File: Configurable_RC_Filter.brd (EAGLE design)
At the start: 48.3 x 40.6 mm, 76 parts, among them SW1 DIP-06, SW2 DIP-06, SW3 DIP-06, SW4 DIP-06

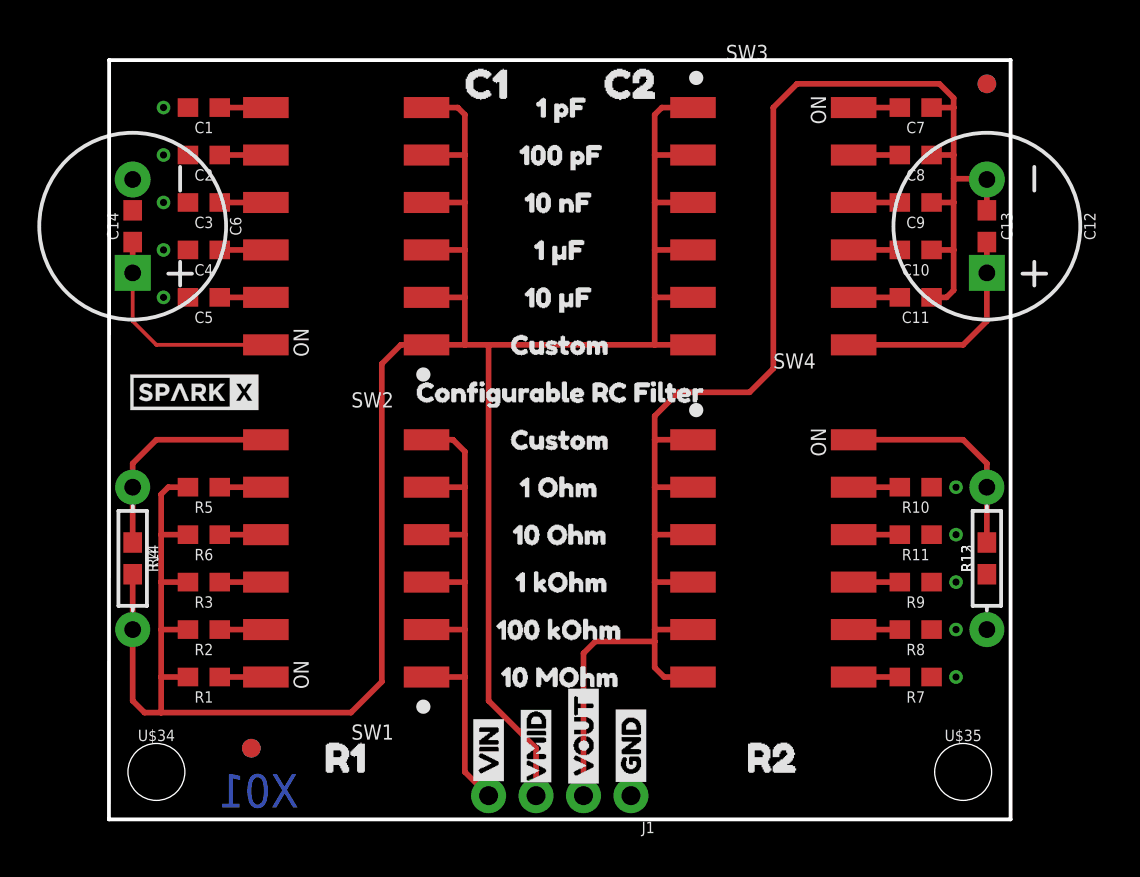
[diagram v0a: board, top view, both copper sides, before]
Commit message: Change cap to NS package.
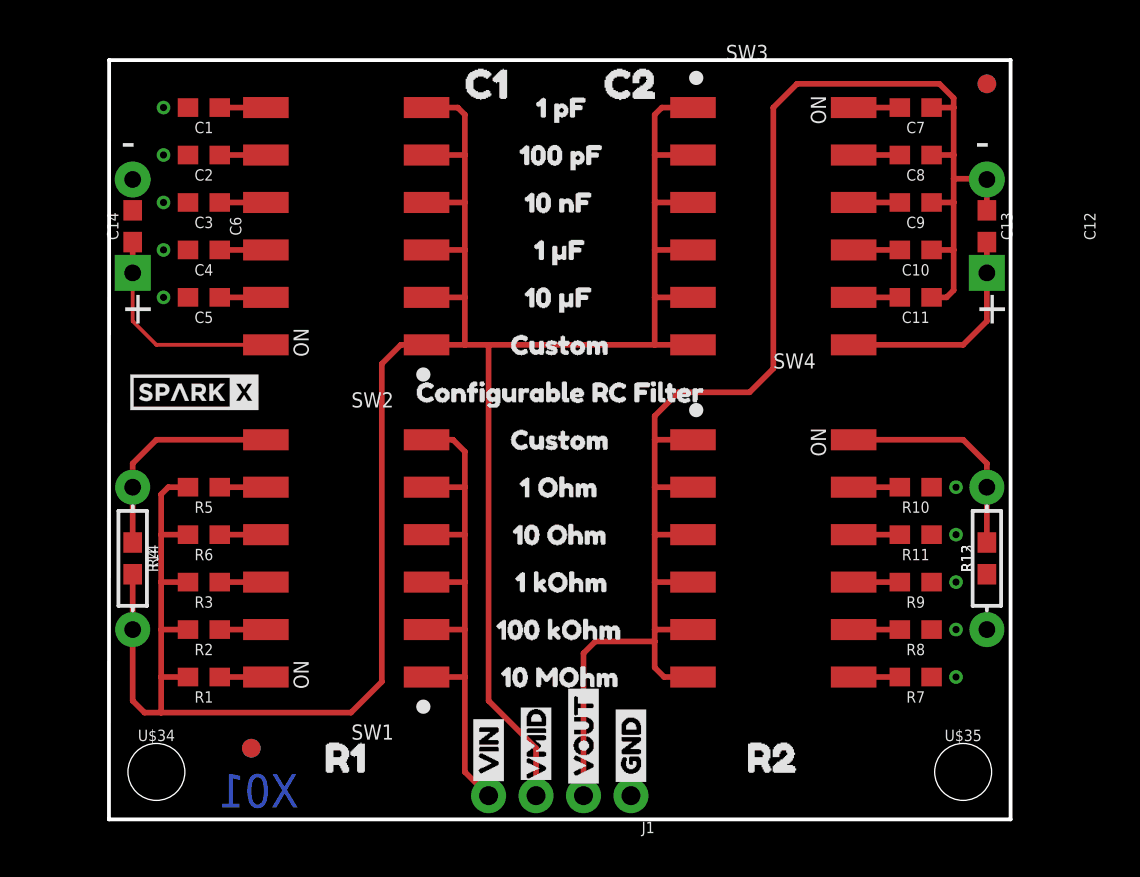
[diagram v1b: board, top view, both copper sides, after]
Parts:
- C12, C6: value 1mF -> 1000UF-RADIAL-5MM-25V-20%-NO-SILK; device SparkFun-Capacitors:CPOL-RADIAL-5MM-10MM -> SparkFun-Capacitors:CPOL-RADIAL-5MM-10MM-NS
- moved U$10 0.13 mm to (22.9, 1.27)
- moved U$9 0.13 mm to (22.9, 1.27)
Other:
- board text added: "+"
- board text added: "-"
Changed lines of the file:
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@@
 <text x="10.16" y="0.635" size="1.778" layer="16" font="vector" ratio="15" rot="MR0">X01</text>
 <text x="25.4" y="-8.89" size="1.778" layer="51" font="vector" ratio="10">Andy England</text>
+<text x="46.355" y="26.543" size="1.778" layer="21" font="vector" ratio="15">+</text>
+<text x="0.635" y="26.543" size="1.778" layer="21" font="vector" ratio="15">+</text>
+<text x="0.635" y="35.433" size="1.778" layer="21" font="vector" ratio="15">-</text>
+<text x="46.355" y="35.433" size="1.778" layer="21" font="vector" ratio="15">-</text>
 </plain>
 <attributes>
@@
 <attribute name="VALUE" x="5.08" y="28.702" size="0.6096" layer="27" font="vector" ratio="20" rot="R180" align="top-center"/>
 </element>
-<element name="C6" library="SparkFun-Capacitors" package="CPOL-RADIAL-5MM-10MM" value="1mF" x="1.27" y="31.75" smashed="yes" rot="R270">
+<element name="C6" library="SparkFun-Capacitors" package="CPOL-RADIAL-5MM-10MM-NS" value="1000UF-RADIAL-5MM-25V-20%-NO-SILK" x="1.27" y="31.75" smashed="yes" rot="R270">
 <attribute name="NAME" x="6.477" y="31.75" size="0.6096" layer="25" font="vector" ratio="20" rot="R270" align="bottom-center"/>
-<attribute name="PROD_ID" value="CAP-09538" x="1.27" y="31.75" size="1.778" layer="27" rot="R270" display="off"/>
-<attribute name="VALUE" x="-3.937" y="31.75" size="0.6096" layer="27" font="vector" ratio="20" rot="R270" align="top-center"/>
 </element>
 <element name="SW3" library="SparkFun-Switches" package="DIPSWITCH-06-SMD" value="DIP-06" x="35.56" y="31.75" smashed="yes" rot="R270">
@@
 <attribute name="VALUE" x="43.18" y="28.702" size="0.6096" layer="27" font="vector" ratio="20" rot="R180" align="top-center"/>
 </element>
-<element name="C12" library="SparkFun-Capacitors" package="CPOL-RADIAL-5MM-10MM" value="1mF" x="46.99" y="31.75" smashed="yes" rot="R270">
+<element name="C12" library="SparkFun-Capacitors" package="CPOL-RADIAL-5MM-10MM-NS" value="1000UF-RADIAL-5MM-25V-20%-NO-SILK" x="46.99" y="31.75" smashed="yes" rot="R270">
 <attribute name="NAME" x="52.197" y="31.75" size="0.6096" layer="25" font="vector" ratio="20" rot="R270" align="bottom-center"/>
-<attribute name="PROD_ID" value="CAP-09538" x="30.48" y="43.18" size="1.778" layer="27" rot="R270" display="off"/>
-<attribute name="VALUE" x="41.783" y="31.75" size="0.6096" layer="27" font="vector" ratio="20" rot="R270" align="top-center"/>
 </element>
 <element name="SW4" library="SparkFun-Switches" package="DIPSWITCH-06-SMD" value="DIP-06" x="35.56" y="13.97" smashed="yes" rot="R270">
@@
 <element name="U$7" library="buzzard_labels (7)" package="VIN1" value="" x="20.32" y="1.524" smashed="yes" rot="R90"/>
 <element name="U$8" library="buzzard_labels (7)" package="VIN1" value="" x="20.32" y="1.524" smashed="yes" rot="MR90"/>
-<element name="U$9" library="buzzard_labels (7)" package="VMID3" value="" x="22.86" y="1.143" smashed="yes" rot="R90"/>
-<element name="U$10" library="buzzard_labels (7)" package="VMID3" value="" x="22.86" y="1.143" smashed="yes" rot="MR90"/>
+<element name="U$9" library="buzzard_labels (7)" package="VMID3" value="" x="22.86" y="1.27" smashed="yes" rot="R90"/>
+<element name="U$10" library="buzzard_labels (7)" package="VMID3" value="" x="22.86" y="1.27" smashed="yes" rot="MR90"/>
 <element name="U$11" library="buzzard_labels (8)" package="VOUT3" value="" x="25.4" y="1.397" smashed="yes" rot="R90"/>
 <element name="U$12" library="buzzard_labels (8)" package="VOUT3" value="" x="25.4" y="1.397" smashed="yes" rot="MR90"/>
@@
 <contactref element="R13" pad="1"/>
 <contactref element="C14" pad="2"/>
+<wire x1="44.03" y1="17.78" x2="45.339" y2="17.78" width="0" layer="19" extent="1-1"/>
+<wire x1="45.339" y1="15.24" x2="45.339" y2="17.78" width="0" layer="19" extent="1-1"/>
+<wire x1="44.03" y1="15.24" x2="45.339" y2="15.24" width="0" layer="19" extent="1-1"/>
+<wire x1="45.339" y1="12.7" x2="45.339" y2="15.24" width="0" layer="19" extent="1-1"/>
+<wire x1="44.03" y1="12.7" x2="45.339" y2="12.7" width="0" layer="19" extent="1-1"/>
+<wire x1="46.99" y1="13.12" x2="45.339" y2="12.7" width="0" layer="19" extent="1-1"/>
+<wire x1="45.339" y1="10.16" x2="45.339" y2="12.7" width="0" layer="19" extent="1-1"/>
+<wire x1="44.03" y1="10.16" x2="45.339" y2="10.16" width="0" layer="19" extent="1-1"/>
+<wire x1="46.99" y1="10.16" x2="45.339" y2="10.16" width="0" layer="19" extent="1-1"/>
+<wire x1="45.339" y1="7.62" x2="45.339" y2="10.16" width="0" layer="19" extent="1-1"/>
+<wire x1="44.03" y1="7.62" x2="45.339" y2="7.62" width="0" layer="19" extent="1-1"/>
+<wire x1="27.94" y1="1.27" x2="44.03" y2="7.62" width="0" layer="19" extent="1-1"/>
+<wire x1="4.23" y1="27.94" x2="27.94" y2="1.27" width="0" layer="19" extent="1-1"/>
+<wire x1="2.921" y1="27.94" x2="4.23" y2="27.94" width="0" layer="19" extent="1-1"/>
+<wire x1="4.23" y1="30.48" x2="4.23" y2="27.94" width="0" layer="19" extent="1-1"/>
+<wire x1="2.921" y1="30.48" x2="4.23" y2="30.48" width="0" layer="19" extent="1-1"/>
+<wire x1="4.23" y1="33.02" x2="4.23" y2="30.48" width="0" layer="19" extent="1-1"/>
+<wire x1="2.921" y1="33.02" x2="4.23" y2="33.02" width="0" layer="19" extent="1-1"/>
+<wire x1="1.27" y1="32.6" x2="2.921" y2="33.02" width="0" layer="19" extent="1-1"/>
+<wire x1="1.27" y1="34.25" x2="1.27" y2="32.6" width="0" layer="19" extent="1-1"/>
+<wire x1="2.921" y1="35.56" x2="1.27" y2="34.25" width="0" layer="19" extent="1-1"/>
+<wire x1="4.23" y1="35.56" x2="2.921" y2="35.56" width="0" layer="19" extent="1-1"/>
+<wire x1="4.23" y1="38.1" x2="4.23" y2="35.56" width="0" layer="19" extent="1-1"/>
+<wire x1="2.921" y1="38.1" x2="4.23" y2="38.1" width="0" layer="19" extent="1-1"/>
 </signal>
 <signal name="VDDA">
